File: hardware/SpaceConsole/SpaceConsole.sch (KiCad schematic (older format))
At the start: 10 parts, among them IC1 ArduinoProMini, J1 Screw_Terminal_01x03, J2 Screw_Terminal_01x03, J3 Screw_Terminal_01x03, J4 Screw_Terminal_01x03, J5 Screw_Terminal_01x03, J6 Screw_Terminal_01x02, J7 Screw_Terminal_01x02

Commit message: Add footprints for all components (except Buck)
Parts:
- IC1: footprint mysensors_arduino:pro_mini_china -> mysensors_arduino:pro_mini
- J1, J2, J3, J4, J5: footprint (none) -> TerminalBlock_RND:TerminalBlock_RND_205-00046_1x03_P5.00mm_Horizontal
- J6, J7: footprint (none) -> TerminalBlock_RND:TerminalBlock_RND_205-00045_1x02_P5.00mm_Horizontal
- J8: renamed from J?; footprint (none) -> Connector_PinHeader_2.54mm:PinHeader_1x09_P2.54mm_Vertical
- gave numbers to parts that had none: 1
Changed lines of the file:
@@
 F 0 "IC1" H 5300 5600 40  0000 C CNN
 F 1 "ArduinoProMini" H 5300 5524 40  0000 C CNN
-F 2 "mysensors_arduino:pro_mini_china" H 5250 4150 30  0001 C CIN
+F 2 "mysensors_arduino:pro_mini" H 5250 4150 30  0001 C CIN
 F 3 "http://www.arduino.cc/en/uploads/Main/Arduino-Pro-Mini-schematic.pdf" H 5300 5433 60  0000 C CNN
 	1    5250 4150
@@
 F 0 "J1" H 8130 3042 50  0000 L CNN
 F 1 "Screw_Terminal_01x03" H 8130 2951 50  0000 L CNN
-F 2 "" H 8050 3000 50  0001 C CNN
+F 2 "TerminalBlock_RND:TerminalBlock_RND_205-00046_1x03_P5.00mm_Horizontal" H 8050 3000 50  0001 C CNN
 F 3 "~" H 8050 3000 50  0001 C CNN
 	1    8050 3000
@@
 F 0 "J2" H 8130 3392 50  0000 L CNN
 F 1 "Screw_Terminal_01x03" H 8130 3301 50  0000 L CNN
-F 2 "" H 8050 3350 50  0001 C CNN
+F 2 "TerminalBlock_RND:TerminalBlock_RND_205-00046_1x03_P5.00mm_Horizontal" H 8050 3350 50  0001 C CNN
 F 3 "~" H 8050 3350 50  0001 C CNN
 	1    8050 3350
@@
 F 0 "J3" H 8130 3742 50  0000 L CNN
 F 1 "Screw_Terminal_01x03" H 8130 3651 50  0000 L CNN
-F 2 "" H 8050 3700 50  0001 C CNN
+F 2 "TerminalBlock_RND:TerminalBlock_RND_205-00046_1x03_P5.00mm_Horizontal" H 8050 3700 50  0001 C CNN
 F 3 "~" H 8050 3700 50  0001 C CNN
 	1    8050 3700
@@
 F 0 "J4" H 8130 4092 50  0000 L CNN
 F 1 "Screw_Terminal_01x03" H 8130 4001 50  0000 L CNN
-F 2 "" H 8050 4050 50  0001 C CNN
+F 2 "TerminalBlock_RND:TerminalBlock_RND_205-00046_1x03_P5.00mm_Horizontal" H 8050 4050 50  0001 C CNN
 F 3 "~" H 8050 4050 50  0001 C CNN
 	1    8050 4050
@@
 F 0 "J5" H 8130 4492 50  0000 L CNN
 F 1 "Screw_Terminal_01x03" H 8130 4401 50  0000 L CNN
-F 2 "" H 8050 4450 50  0001 C CNN
+F 2 "TerminalBlock_RND:TerminalBlock_RND_205-00046_1x03_P5.00mm_Horizontal" H 8050 4450 50  0001 C CNN
 F 3 "~" H 8050 4450 50  0001 C CNN
 	1    8050 4450
@@
 F 0 "J6" H 8130 4792 50  0000 L CNN
 F 1 "Screw_Terminal_01x02" H 8130 4701 50  0000 L CNN
-F 2 "" H 8050 4800 50  0001 C CNN
+F 2 "TerminalBlock_RND:TerminalBlock_RND_205-00045_1x02_P5.00mm_Horizontal" H 8050 4800 50  0001 C CNN
 F 3 "~" H 8050 4800 50  0001 C CNN
 	1    8050 4800
@@
 F 0 "J7" H 8130 5142 50  0000 L CNN
 F 1 "Screw_Terminal_01x02" H 8130 5051 50  0000 L CNN
-F 2 "" H 8050 5150 50  0001 C CNN
+F 2 "TerminalBlock_RND:TerminalBlock_RND_205-00045_1x02_P5.00mm_Horizontal" H 8050 5150 50  0001 C CNN
 F 3 "~" H 8050 5150 50  0001 C CNN
 	1    8050 5150
@@
 $EndComp
 $Comp
-L power:GND #PWR?
+L power:GND #PWR09
 U 1 1 5FB9B39A
 P 7850 3100
-F 0 "#PWR?" H 7850 2850 50  0001 C CNN
+F 0 "#PWR09" H 7850 2850 50  0001 C CNN
 F 1 "GND" V 7855 2972 50  0000 R CNN
 F 2 "" H 7850 3100 50  0001 C CNN
@@
 $EndComp
 $Comp
-L power:GND #PWR?
+L power:GND #PWR011
 U 1 1 5FB9BFBF
 P 7850 3450
-F 0 "#PWR?" H 7850 3200 50  0001 C CNN
+F 0 "#PWR011" H 7850 3200 50  0001 C CNN
 F 1 "GND" V 7855 3322 50  0000 R CNN
 F 2 "" H 7850 3450 50  0001 C CNN
@@
 $EndComp
 $Comp
-L power:GND #PWR?
+L power:GND #PWR013
 U 1 1 5FB9C2F9
 P 7850 3800
-F 0 "#PWR?" H 7850 3550 50  0001 C CNN
+F 0 "#PWR013" H 7850 3550 50  0001 C CNN
 F 1 "GND" V 7855 3672 50  0000 R CNN
 F 2 "" H 7850 3800 50  0001 C CNN
@@
 $EndComp
 $Comp
-L power:GND #PWR?
+L power:GND #PWR015
 U 1 1 5FB9C647
 P 7850 4150
-F 0 "#PWR?" H 7850 3900 50  0001 C CNN
+F 0 "#PWR015" H 7850 3900 50  0001 C CNN
 F 1 "GND" V 7855 4022 50  0000 R CNN
 F 2 "" H 7850 4150 50  0001 C CNN
@@
 $EndComp
 $Comp
-L power:GND #PWR?
+L power:GND #PWR017
 U 1 1 5FB9CF71
 P 7850 4550
-F 0 "#PWR?" H 7850 4300 50  0001 C CNN
+F 0 "#PWR017" H 7850 4300 50  0001 C CNN
 F 1 "GND" V 7855 4422 50  0000 R CNN
 F 2 "" H 7850 4550 50  0001 C CNN
@@
 $EndComp
 $Comp
-L power:VCC #PWR?
+L power:VCC #PWR08
 U 1 1 5FB9D84A
 P 7850 2900
-F 0 "#PWR?" H 7850 2750 50  0001 C CNN
+F 0 "#PWR08" H 7850 2750 50  0001 C CNN
 F 1 "VCC" V 7865 3027 50  0000 L CNN
 F 2 "" H 7850 2900 50  0001 C CNN
@@
 $EndComp
 $Comp
-L power:VCC #PWR?
+L power:VCC #PWR010
 U 1 1 5FB9E272
 P 7850 3250
-F 0 "#PWR?" H 7850 3100 50  0001 C CNN
+F 0 "#PWR010" H 7850 3100 50  0001 C CNN
 F 1 "VCC" V 7865 3377 50  0000 L CNN
 F 2 "" H 7850 3250 50  0001 C CNN
@@
 $EndComp
 $Comp
-L power:VCC #PWR?
+L power:VCC #PWR012
 U 1 1 5FB9EB8F
 P 7850 3600
-F 0 "#PWR?" H 7850 3450 50  0001 C CNN
+F 0 "#PWR012" H 7850 3450 50  0001 C CNN
 F 1 "VCC" V 7865 3727 50  0000 L CNN
 F 2 "" H 7850 3600 50  0001 C CNN
@@
 $EndComp
 $Comp
-L power:VCC #PWR?
+L power:VCC #PWR014
 U 1 1 5FB9F00F
 P 7850 3950
-F 0 "#PWR?" H 7850 3800 50  0001 C CNN
+F 0 "#PWR014" H 7850 3800 50  0001 C CNN
 F 1 "VCC" V 7865 4077 50  0000 L CNN
 F 2 "" H 7850 3950 50  0001 C CNN
@@
 $EndComp
 $Comp
-L power:VCC #PWR?
+L power:VCC #PWR016
 U 1 1 5FB9F5DF
 P 7850 4350
-F 0 "#PWR?" H 7850 4200 50  0001 C CNN
+F 0 "#PWR016" H 7850 4200 50  0001 C CNN
 F 1 "VCC" V 7865 4477 50  0000 L CNN
 F 2 "" H 7850 4350 50  0001 C CNN
@@
 	7550 3450 7550 3700
 $Comp
-L myComponents:LM2596_Adj_Stepdown_Module U?
+L myComponents:LM2596_Adj_Stepdown_Module U1
 U 1 1 5FBA7ED4
 P 7200 5650
-F 0 "U?" H 7428 5326 50  0000 L CNN
+F 0 "U1" H 7428 5326 50  0000 L CNN
 F 1 "LM2596_Adj_Stepdown_Module" H 7428 5235 50  0000 L CNN
 F 2 "" H 7200 5650 50  0001 C CNN
@@
 $EndComp
 $Comp
-L power:VCC #PWR?
+L power:VCC #PWR06
 U 1 1 5FBA8E0E
 P 6950 6100
-F 0 "#PWR?" H 6950 5950 50  0001 C CNN
+F 0 "#PWR06" H 6950 5950 50  0001 C CNN
 F 1 "VCC" V 6965 6227 50  0000 L CNN
 F 2 "" H 6950 6100 50  0001 C CNN
@@
 $EndComp
 $Comp
-L power:GND #PWR?
+L power:GND #PWR07
 U 1 1 5FBAA224
 P 6950 6250
-F 0 "#PWR?" H 6950 6000 50  0001 C CNN
+F 0 "#PWR07" H 6950 6000 50  0001 C CNN
 F 1 "GND" V 6955 6122 50  0000 R CNN
 F 2 "" H 6950 6250 50  0001 C CNN
@@
 Battery-
 $Comp
-L Connector:Conn_01x09_Male J?
+L Connector:Conn_01x09_Male J8
 U 1 1 5FBB2A1F
 P 5450 6400
-F 0 "J?" H 5558 6981 50  0000 C CNN
+F 0 "J8" H 5558 6981 50  0000 C CNN
 F 1 "Conn_01x09_Male" H 5558 6890 50  0000 C CNN
-F 2 "" H 5450 6400 50  0001 C CNN
+F 2 "Connector_PinHeader_2.54mm:PinHeader_1x09_P2.54mm_Vertical" H 5450 6400 50  0001 C CNN
 F 3 "~" H 5450 6400 50  0001 C CNN
 	1    5450 6400
@@
 $EndComp
 $Comp
-L power:GND #PWR?
+L power:GND #PWR04
 U 1 1 5FBB4227
 P 5650 6000
-F 0 "#PWR?" H 5650 5750 50  0001 C CNN
+F 0 "#PWR04" H 5650 5750 50  0001 C CNN
 F 1 "GND" V 5655 5872 50  0000 R CNN
 F 2 "" H 5650 6000 50  0001 C CNN
@@
 $EndComp
 $Comp
-L power:VCC #PWR?
+L power:VCC #PWR05
 U 1 1 5FBB4E89
 P 5650 6100
-F 0 "#PWR?" H 5650 5950 50  0001 C CNN
+F 0 "#PWR05" H 5650 5950 50  0001 C CNN
 F 1 "VCC" V 5665 6228 50  0000 L CNN
 F 2 "" H 5650 6100 50  0001 C CNN

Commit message: PCB layed out (no traces yet)
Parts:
- J1: value Screw_Terminal_01x03 -> LeftFrontLED
- J2: value Screw_Terminal_01x03 -> RightFrontLED
- J3: value Screw_Terminal_01x03 -> LeftMiddleLED
- J4: value Screw_Terminal_01x03 -> RightMiddleLED
- J5: value Screw_Terminal_01x03 -> RearLED
- J6: value Screw_Terminal_01x02 -> SwitchA
- J7: value Screw_Terminal_01x02 -> BatteryIN
- U1: footprint (none) -> myComponents:LM2596_Adj_Stepdown_Module
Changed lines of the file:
@@
 P 8050 3000
 F 0 "J1" H 8130 3042 50  0000 L CNN
-F 1 "Screw_Terminal_01x03" H 8130 2951 50  0000 L CNN
+F 1 "LeftFrontLED" H 8130 2951 50  0000 L CNN
 F 2 "TerminalBlock_RND:TerminalBlock_RND_205-00046_1x03_P5.00mm_Horizontal" H 8050 3000 50  0001 C CNN
 F 3 "~" H 8050 3000 50  0001 C CNN
@@
 P 8050 3350
 F 0 "J2" H 8130 3392 50  0000 L CNN
-F 1 "Screw_Terminal_01x03" H 8130 3301 50  0000 L CNN
+F 1 "RightFrontLED" H 8130 3301 50  0000 L CNN
 F 2 "TerminalBlock_RND:TerminalBlock_RND_205-00046_1x03_P5.00mm_Horizontal" H 8050 3350 50  0001 C CNN
 F 3 "~" H 8050 3350 50  0001 C CNN
@@
 P 8050 3700
 F 0 "J3" H 8130 3742 50  0000 L CNN
-F 1 "Screw_Terminal_01x03" H 8130 3651 50  0000 L CNN
+F 1 "LeftMiddleLED" H 8130 3651 50  0000 L CNN
 F 2 "TerminalBlock_RND:TerminalBlock_RND_205-00046_1x03_P5.00mm_Horizontal" H 8050 3700 50  0001 C CNN
 F 3 "~" H 8050 3700 50  0001 C CNN
@@
 P 8050 4050
 F 0 "J4" H 8130 4092 50  0000 L CNN
-F 1 "Screw_Terminal_01x03" H 8130 4001 50  0000 L CNN
+F 1 "RightMiddleLED" H 8130 4001 50  0000 L CNN
 F 2 "TerminalBlock_RND:TerminalBlock_RND_205-00046_1x03_P5.00mm_Horizontal" H 8050 4050 50  0001 C CNN
 F 3 "~" H 8050 4050 50  0001 C CNN
@@
 P 8050 4450
 F 0 "J5" H 8130 4492 50  0000 L CNN
-F 1 "Screw_Terminal_01x03" H 8130 4401 50  0000 L CNN
+F 1 "RearLED" H 8130 4401 50  0000 L CNN
 F 2 "TerminalBlock_RND:TerminalBlock_RND_205-00046_1x03_P5.00mm_Horizontal" H 8050 4450 50  0001 C CNN
 F 3 "~" H 8050 4450 50  0001 C CNN
@@
 P 8050 4800
 F 0 "J6" H 8130 4792 50  0000 L CNN
-F 1 "Screw_Terminal_01x02" H 8130 4701 50  0000 L CNN
+F 1 "SwitchA" H 8130 4701 50  0000 L CNN
 F 2 "TerminalBlock_RND:TerminalBlock_RND_205-00045_1x02_P5.00mm_Horizontal" H 8050 4800 50  0001 C CNN
 F 3 "~" H 8050 4800 50  0001 C CNN
@@
 P 8050 5150
 F 0 "J7" H 8130 5142 50  0000 L CNN
-F 1 "Screw_Terminal_01x02" H 8130 5051 50  0000 L CNN
+F 1 "BatteryIN" H 8130 5051 50  0000 L CNN
 F 2 "TerminalBlock_RND:TerminalBlock_RND_205-00045_1x02_P5.00mm_Horizontal" H 8050 5150 50  0001 C CNN
 F 3 "~" H 8050 5150 50  0001 C CNN
@@
 F 0 "U1" H 7428 5326 50  0000 L CNN
 F 1 "LM2596_Adj_Stepdown_Module" H 7428 5235 50  0000 L CNN
-F 2 "" H 7200 5650 50  0001 C CNN
+F 2 "myComponents:LM2596_Adj_Stepdown_Module" H 7200 5650 50  0001 C CNN
 F 3 "" H 7200 5650 50  0001 C CNN
 	1    7200 5650

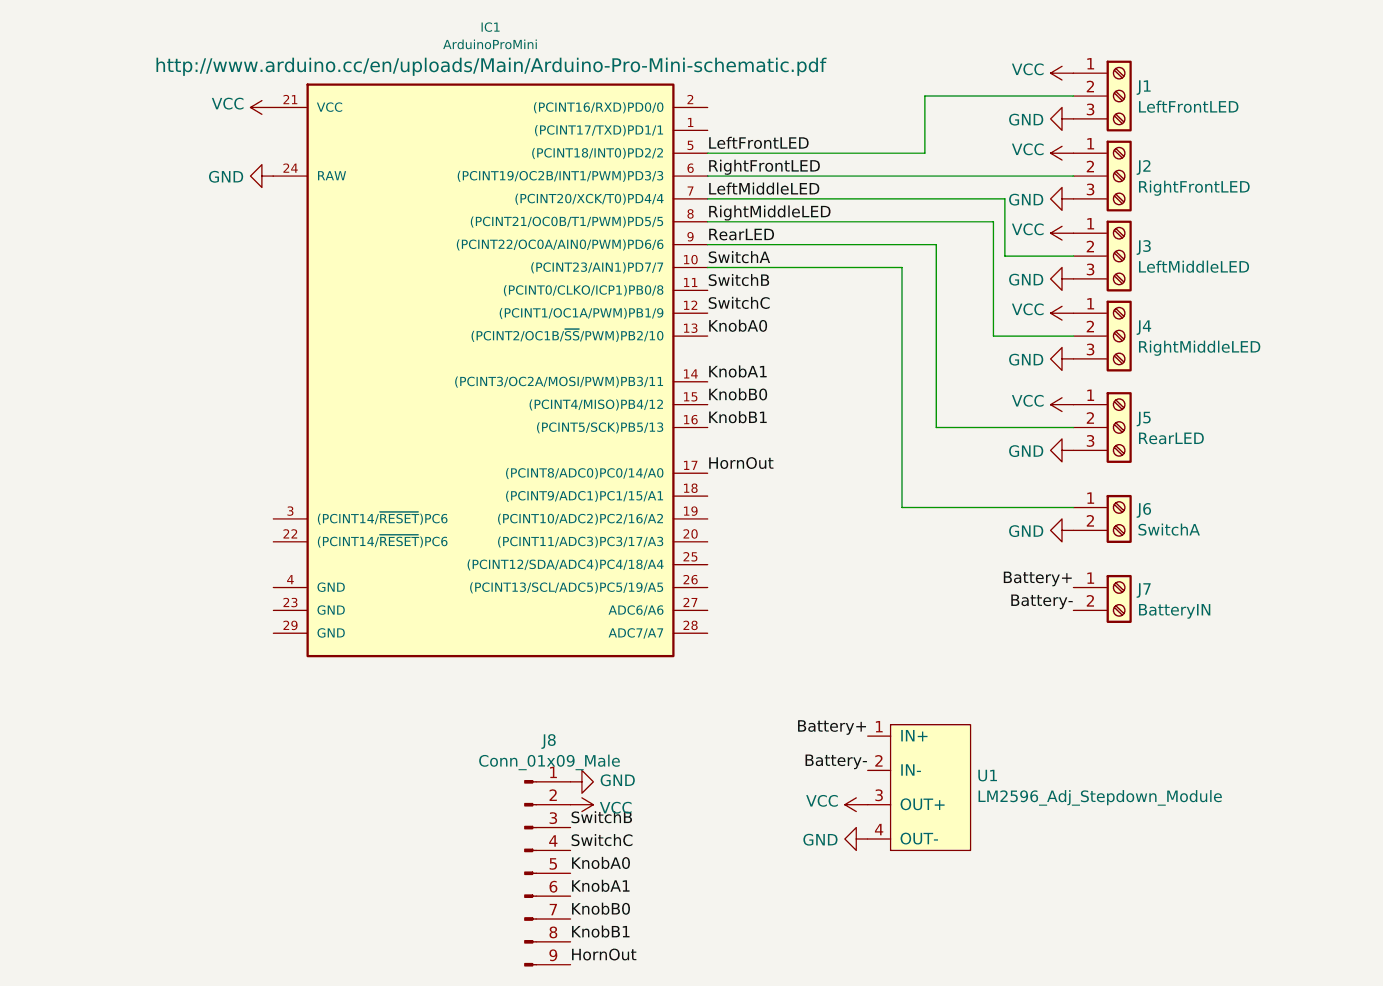
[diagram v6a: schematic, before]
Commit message: Remove extra pins from pro
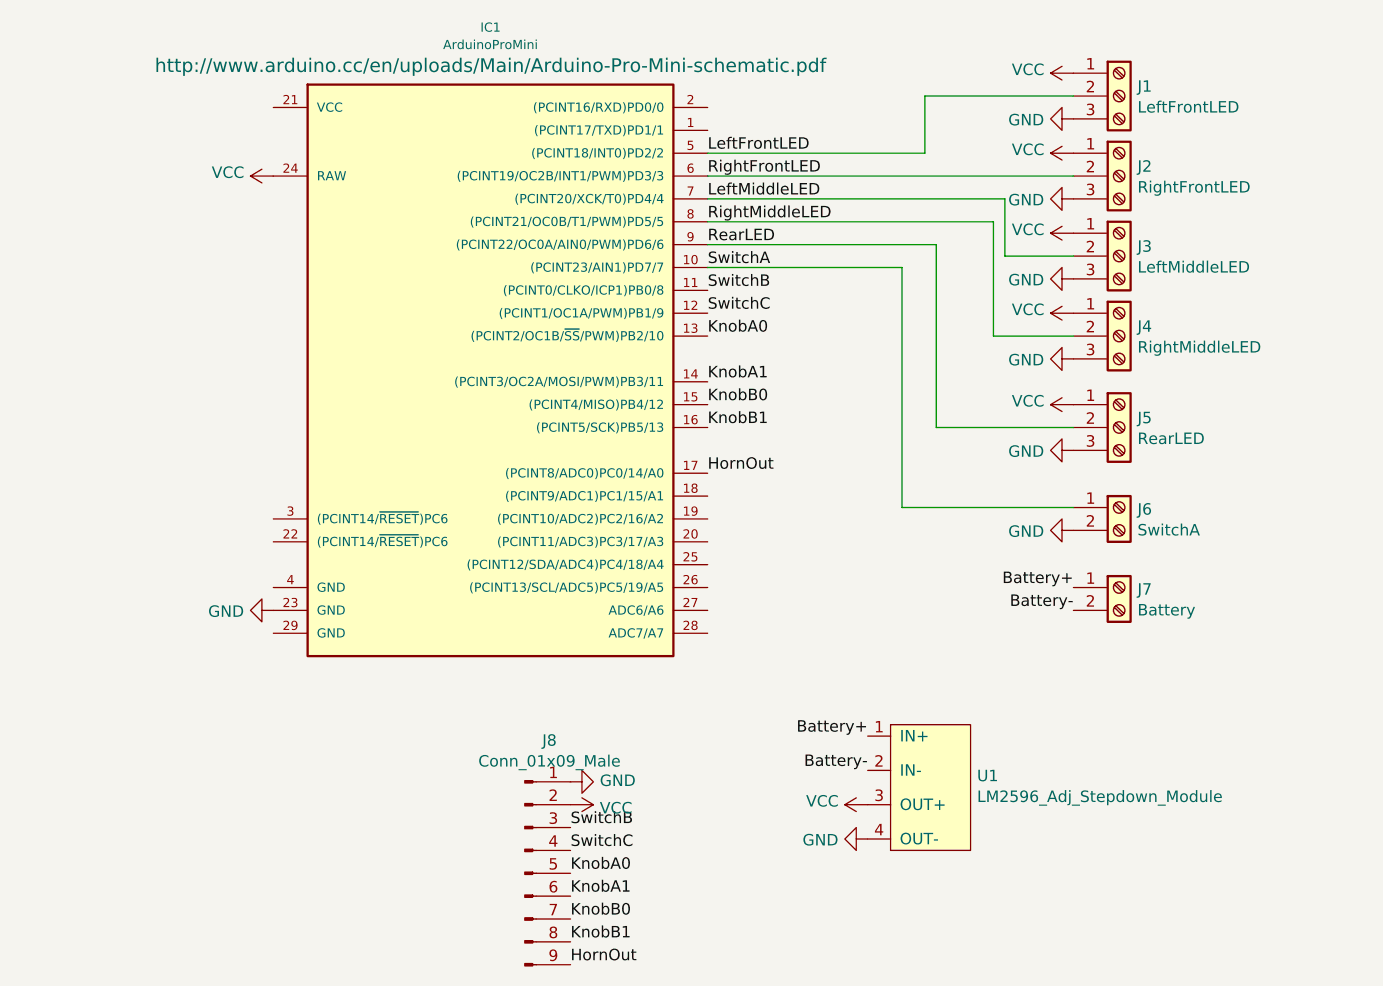
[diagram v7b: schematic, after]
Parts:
- J7: value BatteryIN -> Battery
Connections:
- net GND: now also IC1.23 (GND); no longer IC1.24 (RAW)
- net VCC: now also IC1.24 (RAW); no longer IC1.21 (VCC)
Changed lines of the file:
@@
 L power:VCC #PWR01
 U 1 1 5FB7FD72
-P 4350 3050
-F 0 "#PWR01" H 4350 2900 50  0001 C CNN
-F 1 "VCC" V 4365 3177 50  0000 L CNN
-F 2 "" H 4350 3050 50  0001 C CNN
-F 3 "" H 4350 3050 50  0001 C CNN
-	1    4350 3050
-	0    -1   -1   0
-$EndComp
-$Comp
-L power:GND #PWR02
-U 1 1 5FB80DDB
 P 4350 3350
-F 0 "#PWR02" H 4350 3100 50  0001 C CNN
-F 1 "GND" V 4355 3222 50  0000 R CNN
+F 0 "#PWR01" H 4350 3200 50  0001 C CNN
+F 1 "VCC" V 4365 3477 50  0000 L CNN
 F 2 "" H 4350 3350 50  0001 C CNN
 F 3 "" H 4350 3350 50  0001 C CNN
 	1    4350 3350
-	0    1    1    0
+	0    -1   -1   0
 $EndComp
 Text Label 6250 3250 0    50   ~ 0
@@
 	1    0    0    -1
 $EndComp
-$Comp
-L Connector:Screw_Terminal_01x02 J7
-U 1 1 5FB97F65
-P 8050 5150
-F 0 "J7" H 8130 5142 50  0000 L CNN
-F 1 "BatteryIN" H 8130 5051 50  0000 L CNN
-F 2 "TerminalBlock_RND:TerminalBlock_RND_205-00045_1x02_P5.00mm_Horizontal" H 8050 5150 50  0001 C CNN
-F 3 "~" H 8050 5150 50  0001 C CNN
-	1    8050 5150
-	1    0    0    -1
-$EndComp
 Wire Wire Line
 	6250 3750 7100 3750
@@
 Text Label 5650 6800 0    50   ~ 0
 HornOut
+$Comp
+L Connector:Screw_Terminal_01x02 J7
+U 1 1 5FB97F65
+P 8050 5150
+F 0 "J7" H 8130 5142 50  0000 L CNN
+F 1 "Battery" H 8130 5051 50  0000 L CNN
+F 2 "TerminalBlock_RND:TerminalBlock_RND_205-00045_1x02_P5.00mm_Horizontal" H 8050 5150 50  0001 C CNN
+F 3 "~" H 8050 5150 50  0001 C CNN
+	1    8050 5150
+	1    0    0    -1
+$EndComp
+$Comp
+L power:GND #PWR0101
+U 1 1 5FBFD67E
+P 4350 5250
+F 0 "#PWR0101" H 4350 5000 50  0001 C CNN
+F 1 "GND" V 4355 5122 50  0000 R CNN
+F 2 "" H 4350 5250 50  0001 C CNN
+F 3 "" H 4350 5250 50  0001 C CNN
+	1    4350 5250
+	0    1    1    0
+$EndComp
 $EndSCHEMATC

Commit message: Add power switch
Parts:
- added J9: Power_Switch, Connector_PinHeader_2.54mm:PinHeader_1x02_P2.54mm_Vertical, symbol Connector:Conn_01x02_Male
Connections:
- net Battery+: no longer names the net of J7.1 (Pin_1)
- net Battery+: now also J9.1 (Pin_1); no longer U1.1 (IN+)
- new net: J9.2 (Pin_2), U1.1 (IN+)
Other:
- moved on the sheet: U1
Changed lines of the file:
@@
 L myComponents:LM2596_Adj_Stepdown_Module U1
 U 1 1 5FBA7ED4
-P 7200 5650
-F 0 "U1" H 7428 5326 50  0000 L CNN
-F 1 "LM2596_Adj_Stepdown_Module" H 7428 5235 50  0000 L CNN
-F 2 "myComponents:LM2596_Adj_Stepdown_Module" H 7200 5650 50  0001 C CNN
-F 3 "" H 7200 5650 50  0001 C CNN
-	1    7200 5650
+P 7400 5350
+F 0 "U1" H 7628 5026 50  0000 L CNN
+F 1 "LM2596_Adj_Stepdown_Module" H 7628 4935 50  0000 L CNN
+F 2 "myComponents:LM2596_Adj_Stepdown_Module" H 7400 5350 50  0001 C CNN
+F 3 "" H 7400 5350 50  0001 C CNN
+	1    7400 5350
 	1    0    0    -1
 $EndComp
@@
 L power:VCC #PWR06
 U 1 1 5FBA8E0E
-P 6950 6100
-F 0 "#PWR06" H 6950 5950 50  0001 C CNN
-F 1 "VCC" V 6965 6227 50  0000 L CNN
-F 2 "" H 6950 6100 50  0001 C CNN
-F 3 "" H 6950 6100 50  0001 C CNN
-	1    6950 6100
+P 7150 5800
+F 0 "#PWR06" H 7150 5650 50  0001 C CNN
+F 1 "VCC" V 7165 5927 50  0000 L CNN
+F 2 "" H 7150 5800 50  0001 C CNN
+F 3 "" H 7150 5800 50  0001 C CNN
+	1    7150 5800
 	0    -1   -1   0
 $EndComp
@@
 L power:GND #PWR07
 U 1 1 5FBAA224
-P 6950 6250
-F 0 "#PWR07" H 6950 6000 50  0001 C CNN
-F 1 "GND" V 6955 6122 50  0000 R CNN
-F 2 "" H 6950 6250 50  0001 C CNN
-F 3 "" H 6950 6250 50  0001 C CNN
-	1    6950 6250
+P 7150 5950
+F 0 "#PWR07" H 7150 5700 50  0001 C CNN
+F 1 "GND" V 7155 5822 50  0000 R CNN
+F 2 "" H 7150 5950 50  0001 C CNN
+F 3 "" H 7150 5950 50  0001 C CNN
+	1    7150 5950
 	0    1    1    0
 $EndComp
-Text Label 7850 5150 2    50   ~ 0
-Battery+
-Text Label 6950 5800 2    50   ~ 0
-Battery+
 Text Label 7850 5250 2    50   ~ 0
 Battery-
-Text Label 6950 5950 2    50   ~ 0
+Text Label 7150 5650 2    50   ~ 0
 Battery-
 $Comp
@@
 	0    1    1    0
 $EndComp
+$Comp
+L Connector:Conn_01x02_Male J9
+U 1 1 5FC093C0
+P 6700 5400
+F 0 "J9" H 6808 5581 50  0000 C CNN
+F 1 "Power_Switch" H 6808 5490 50  0000 C CNN
+F 2 "Connector_PinHeader_2.54mm:PinHeader_1x02_P2.54mm_Vertical" H 6700 5400 50  0001 C CNN
+F 3 "~" H 6700 5400 50  0001 C CNN
+	1    6700 5400
+	1    0    0    -1
+$EndComp
+Wire Wire Line
+	6900 5400 6900 5150
+Wire Wire Line
+	6900 5150 7850 5150
+Wire Wire Line
+	6900 5500 7150 5500
 $EndSCHEMATC
